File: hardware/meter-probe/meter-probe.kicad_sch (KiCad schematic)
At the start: 49 parts, among them J1 Cable, SW1 Sensor Button, U1 TSL2585, U2 USBLC6-2SC6, U3 MIC5365-1.8YC5, U4 FT260Q, U5 CAT24C08

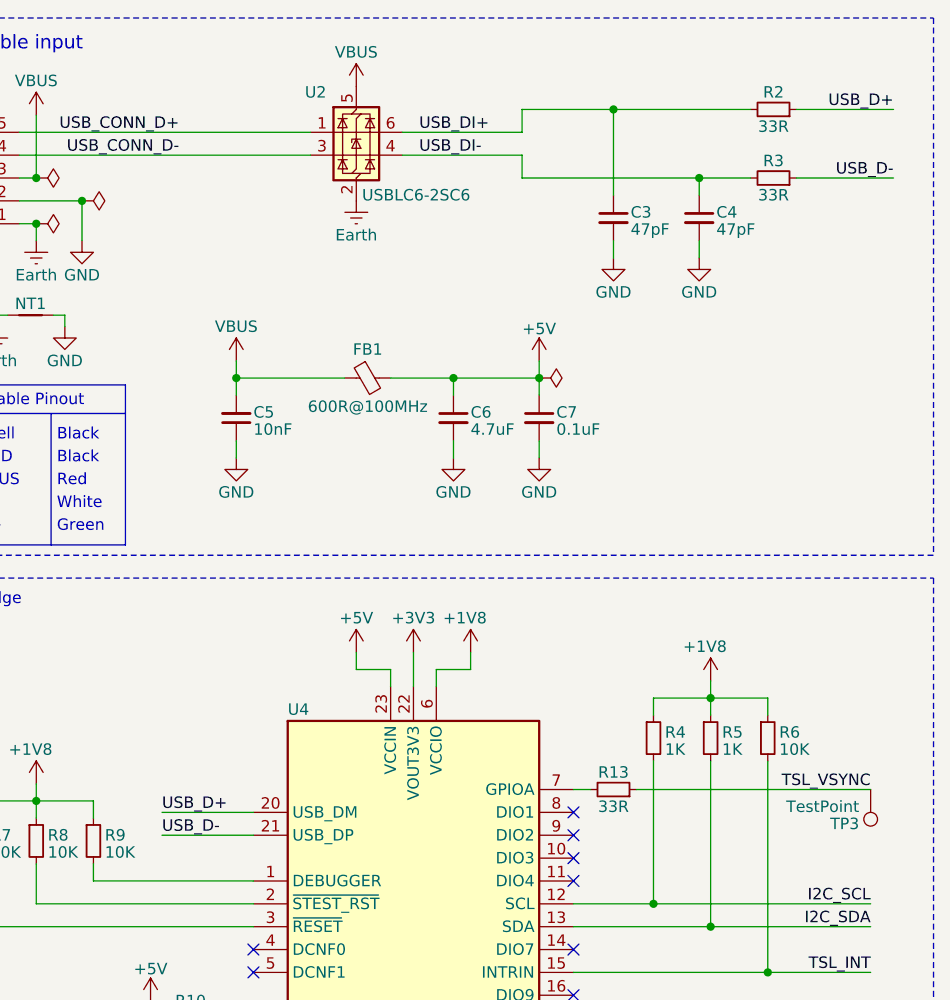
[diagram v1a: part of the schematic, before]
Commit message: Fix pin swap with USB cable connector
This adds vias to the USB traces, which we normally try to avoid, but
that's the only way to route it. Hopefully it won't cause any issues.

Fix #51
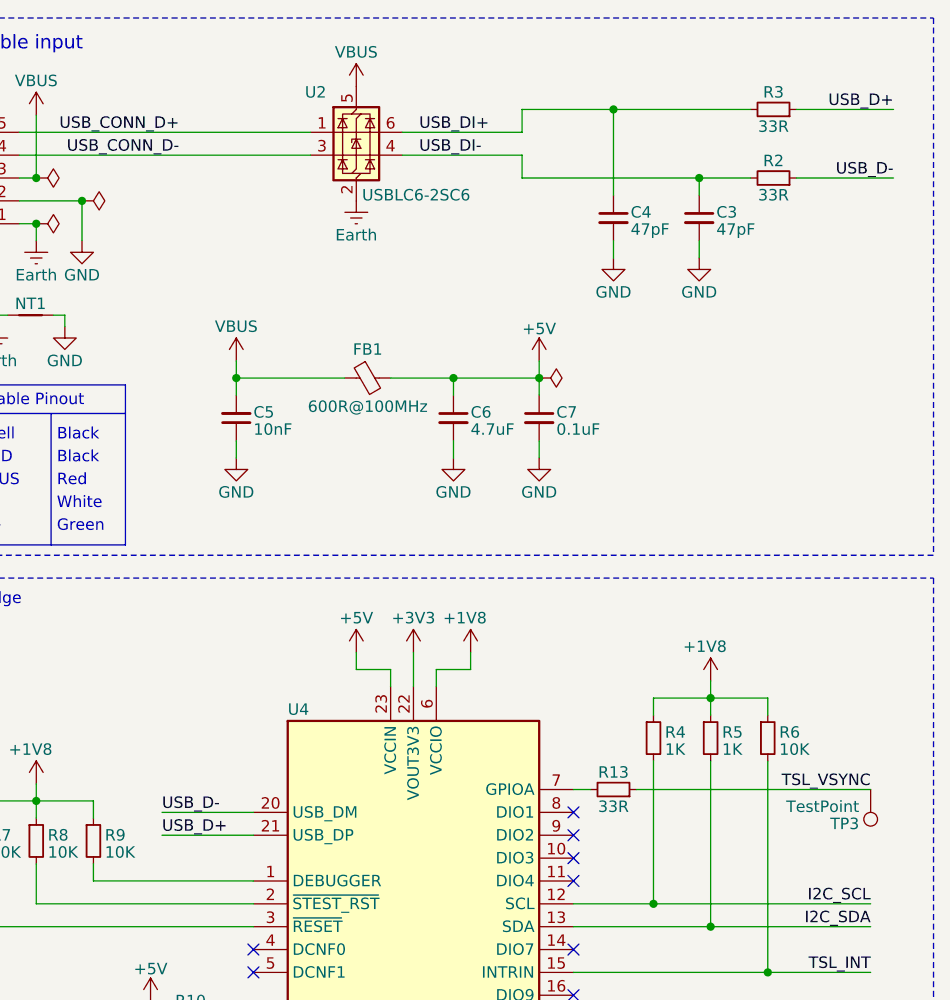
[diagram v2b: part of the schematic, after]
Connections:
- net USB_D+: now also R3.1, U4.21 (USB_DP); no longer R2.1, U4.20 (USB_DM)
- net USB_D-: now also R2.1, U4.20 (USB_DM); no longer R3.1, U4.21 (USB_DP)
- net USB_DI+: now also C4.1, R3.2; no longer C3.1, R2.2
- net USB_DI-: now also C3.1, R2.2; no longer C4.1, R3.2
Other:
- moved on the sheet: C3, C4, R2, R3
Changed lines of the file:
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@@
 	(title_block
 		(title "Printalyzer - Meter Probe")
-		(date "2024-02-27")
+		(date "2024-04-16")
 		(rev "E")
 		(company "Dektronics, Inc.")
@@
 	)
 	(label "USB_D+"
-		(at 41.275 102.87 0)
+		(at 41.275 105.41 0)
 		(fields_autoplaced yes)
 		(effects
@@
 	)
 	(label "USB_D-"
-		(at 41.275 105.41 0)
+		(at 41.275 102.87 0)
 		(fields_autoplaced yes)
 		(effects
@@
 	(symbol
 		(lib_id "Device:C_Small")
-		(at 91.44 36.83 0)
+		(at 100.965 36.83 0)
 		(mirror y)
 		(unit 1)
@@
 		(dnp no)
 		(property "Reference" "C3"
-			(at 93.345 36.195 0)
+			(at 102.87 36.195 0)
 			(effects
 				(font
@@
 		)
 		(property "Value" "47pF"
-			(at 93.345 38.1 0)
+			(at 102.87 38.1 0)
 			(effects
 				(font
@@
 		)
 		(property "Footprint" "Capacitor_SMD:C_0603_1608Metric"
-			(at 91.44 36.83 0)
+			(at 100.965 36.83 0)
 			(effects
 				(font
@@
 		)
 		(property "Datasheet" "https://www.yageo.com/upload/media/product/productsearch/datasheet/mlcc/UPY-GP_NP0_16V-to-50V_18.pdf"
-			(at 91.44 36.83 0)
+			(at 100.965 36.83 0)
 			(effects
 				(font
@@
 		)
 		(property "Description" "CAP CER 47PF 50V C0G/NPO 0603"
-			(at 91.44 36.83 0)
+			(at 100.965 36.83 0)
 			(effects
 				(font
@@
 		)
 		(property "Manufacturer" "YAGEO"
-			(at 91.44 36.83 0)
+			(at 100.965 36.83 0)
 			(effects
 				(font
@@
 		)
 		(property "Manufacturer PN" "CC0603JRNPO9BN470"
-			(at 91.44 36.83 0)
+			(at 100.965 36.83 0)
 			(effects
 				(font
@@
 		)
 		(property "Supplier" "Digi-Key"
-			(at 91.44 36.83 0)
+			(at 100.965 36.83 0)
 			(effects
 				(font
@@
 		)
 		(property "Supplier PN" "311-1065-1-ND"
-			(at 91.44 36.83 0)
+			(at 100.965 36.83 0)
 			(effects
 				(font
@@
 	(symbol
 		(lib_id "Device:C_Small")
-		(at 100.965 36.83 0)
+		(at 91.44 36.83 0)
 		(mirror y)
 		(unit 1)
@@
 		(dnp no)
 		(property "Reference" "C4"
-			(at 102.87 36.195 0)
+			(at 93.345 36.195 0)
 			(effects
 				(font
@@
 		)
 		(property "Value" "47pF"
-			(at 102.87 38.1 0)
+			(at 93.345 38.1 0)
 			(effects
 				(font
@@
 		)
 		(property "Footprint" "Capacitor_SMD:C_0603_1608Metric"
-			(at 100.965 36.83 0)
+			(at 91.44 36.83 0)
 			(effects
 				(font
@@
 		)
 		(property "Datasheet" "https://www.yageo.com/upload/media/product/productsearch/datasheet/mlcc/UPY-GP_NP0_16V-to-50V_18.pdf"
-			(at 100.965 36.83 0)
+			(at 91.44 36.83 0)
 			(effects
 				(font
@@
 		)
 		(property "Description" "CAP CER 47PF 50V C0G/NPO 0603"
-			(at 100.965 36.83 0)
+			(at 91.44 36.83 0)
 			(effects
 				(font
@@
 		)
 		(property "Manufacturer" "YAGEO"
-			(at 100.965 36.83 0)
+			(at 91.44 36.83 0)
 			(effects
 				(font
@@
 		)
 		(property "Manufacturer PN" "CC0603JRNPO9BN470"
-			(at 100.965 36.83 0)
+			(at 91.44 36.83 0)
 			(effects
 				(font
@@
 		)
 		(property "Supplier" "Digi-Key"
-			(at 100.965 36.83 0)
+			(at 91.44 36.83 0)
 			(effects
 				(font
@@
 		)
 		(property "Supplier PN" "311-1065-1-ND"
-			(at 100.965 36.83 0)
+			(at 91.44 36.83 0)
 			(effects
 				(font
@@
 	(symbol
 		(lib_id "Device:R_Small")
-		(at 109.22 24.765 270)
+		(at 109.22 32.385 270)
 		(mirror x)
 		(unit 1)
@@
 		(dnp no)
 		(property "Reference" "R2"
-			(at 109.22 22.86 90)
+			(at 109.22 30.48 90)
 			(effects
 				(font
@@
 		)
 		(property "Value" "33R"
-			(at 109.22 26.67 90)
+			(at 109.22 34.29 90)
 			(effects
 				(font
@@
 		)
 		(property "Footprint" "Resistor_SMD:R_0603_1608Metric"
-			(at 109.22 26.543 90)
+			(at 109.22 34.163 90)
 			(effects
 				(font
@@
 		)
 		(property "Datasheet" "https://www.yageo.com/upload/media/product/productsearch/datasheet/rchip/PYu-RC_Group_51_RoHS_L_12.pdf"
-			(at 109.22 24.765 0)
+			(at 109.22 32.385 0)
 			(effects
 				(font
@@
 		)
 		(property "Description" "RES 33 OHM 5% 1/10W 0603"
-			(at 109.22 24.765 0)
+			(at 109.22 32.385 0)
 			(effects
 				(font
@@
 		)
 		(property "Manufacturer" "YAGEO"
-			(at 109.22 24.765 0)
+			(at 109.22 32.385 0)
 			(effects
 				(font
@@
 		)
 		(property "Manufacturer PN" "RC0603JR-0733RL"
-			(at 109.22 24.765 0)
+			(at 109.22 32.385 0)
 			(effects
 				(font
@@
 		)
 		(property "Supplier" "Digi-Key"
-			(at 109.22 24.765 0)
+			(at 109.22 32.385 0)
 			(effects
 				(font
@@
 		)
 		(property "Supplier PN" "311-33GRCT-ND"
-			(at 109.22 24.765 0)
+			(at 109.22 32.385 0)
 			(effects
 				(font
@@
 	(symbol
 		(lib_id "Device:R_Small")
-		(at 109.22 32.385 270)
+		(at 109.22 24.765 270)
 		(mirror x)
 		(unit 1)
@@
 		(dnp no)
 		(property "Reference" "R3"
-			(at 109.22 30.48 90)
+			(at 109.22 22.86 90)
 			(effects
 				(font
@@
 		)
 		(property "Value" "33R"
-			(at 109.22 34.29 90)
+			(at 109.22 26.67 90)
 			(effects
 				(font
@@
 		)
 		(property "Footprint" "Resistor_SMD:R_0603_1608Metric"
-			(at 109.22 34.163 90)
+			(at 109.22 26.543 90)
 			(effects
 				(font
@@
 		)
 		(property "Datasheet" "https://www.yageo.com/upload/media/product/productsearch/datasheet/rchip/PYu-RC_Group_51_RoHS_L_12.pdf"
-			(at 109.22 32.385 0)
+			(at 109.22 24.765 0)
 			(effects
 				(font
@@
 		)
 		(property "Description" "RES 33 OHM 5% 1/10W 0603"
-			(at 109.22 32.385 0)
+			(at 109.22 24.765 0)
 			(effects
 				(font
@@
 		)
 		(property "Manufacturer" "YAGEO"
-			(at 109.22 32.385 0)
+			(at 109.22 24.765 0)
 			(effects
 				(font
@@
 		)
 		(property "Manufacturer PN" "RC0603JR-0733RL"
-			(at 109.22 32.385 0)
+			(at 109.22 24.765 0)
 			(effects
 				(font
@@
 		)
 		(property "Supplier" "Digi-Key"
-			(at 109.22 32.385 0)
+			(at 109.22 24.765 0)
 			(effects
 				(font
@@
 		)
 		(property "Supplier PN" "311-33GRCT-ND"
-			(at 109.22 32.385 0)
+			(at 109.22 24.765 0)
 			(effects
 				(font

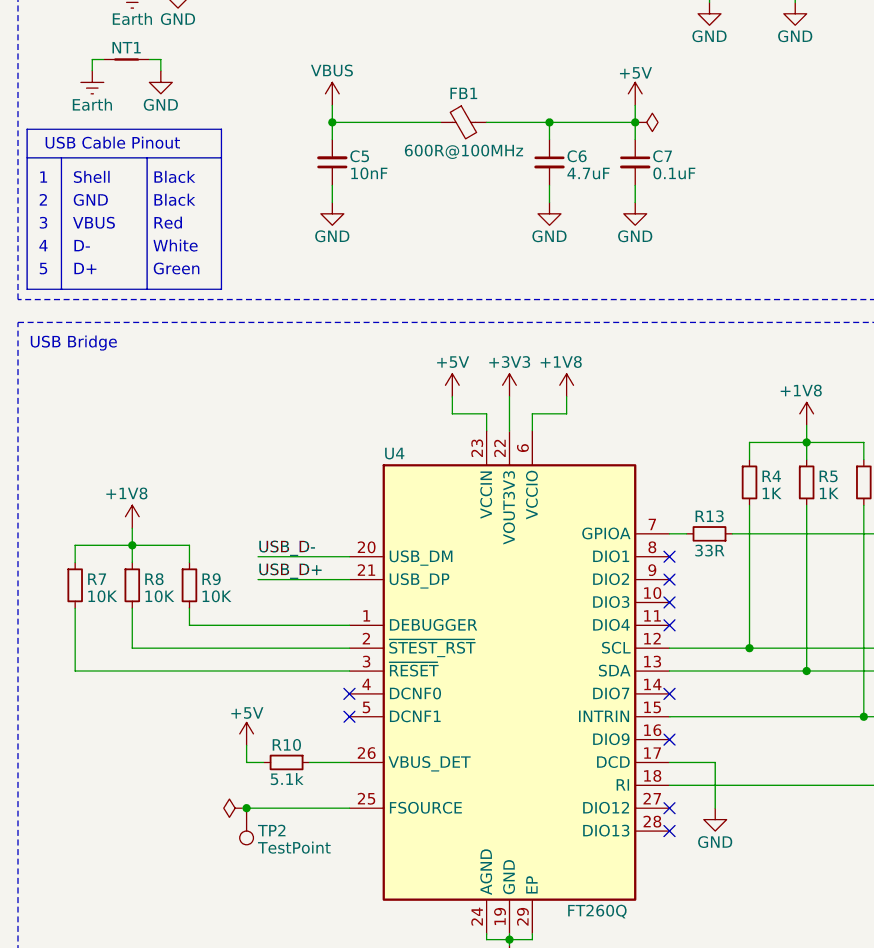
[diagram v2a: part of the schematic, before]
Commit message: Update power input and reset line components
Ref #65
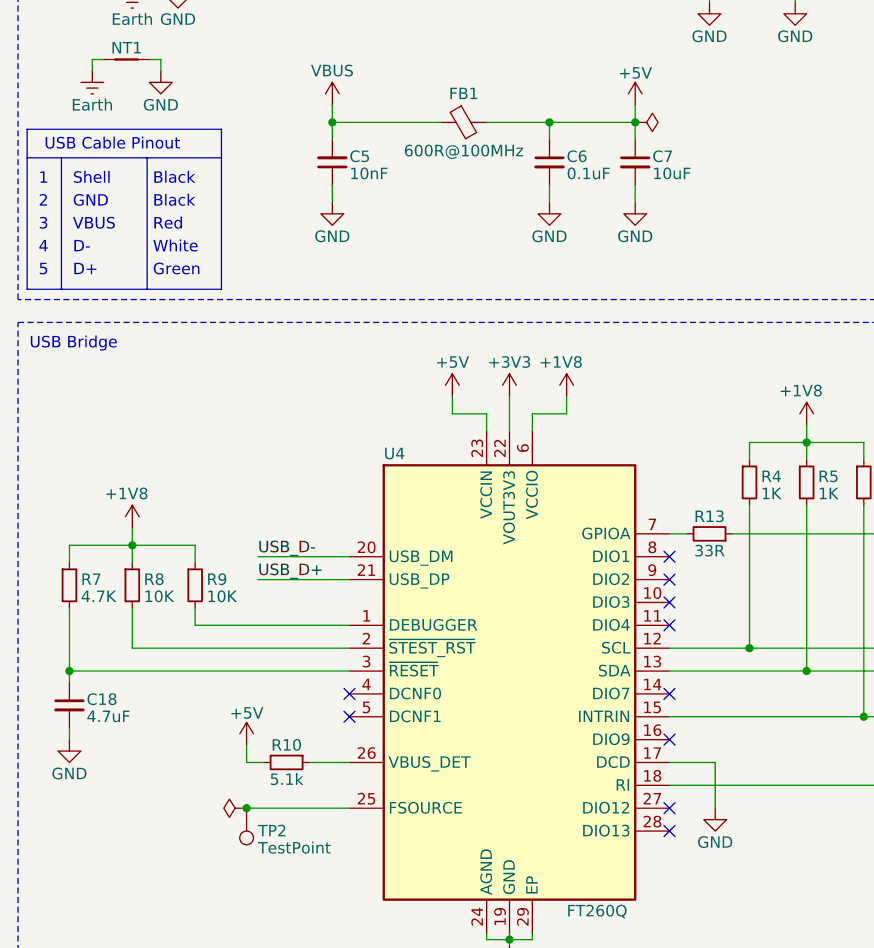
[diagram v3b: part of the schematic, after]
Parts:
- added C18: 4.7uF, Capacitor_SMD:C_0603_1608Metric, symbol Device:C_Small
- C6: value 4.7uF -> 0.1uF; Manufacturer PN CL10A475KA8NQNC -> CL10B104KA8NNNC; Supplier LCSC -> Digi-Key; Supplier PN C69335 -> 1276-1006-1-ND
- C7: value 0.1uF -> 10uF; footprint Capacitor_SMD:C_0603_1608Metric -> Capacitor_SMD:C_0805_2012Metric; Manufacturer PN CL10B104KA8NNNC -> CL21A106KAYNNNE; Supplier PN 1276-1006-1-ND -> 1276-2891-1-ND
- R7: value 10K -> 4.7K; Manufacturer Vishay Dale -> YAGEO; Manufacturer PN CRCW060310K0JNEA -> RC0603JR-074K7L; Supplier PN 541-10KGCT-ND -> 311-4.7KGRCT-ND
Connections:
- net GND: now also C18.2
- net at R7.2, U4.3 (~{RESET}): now also C18.1
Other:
- moved on the sheet: R7, R9

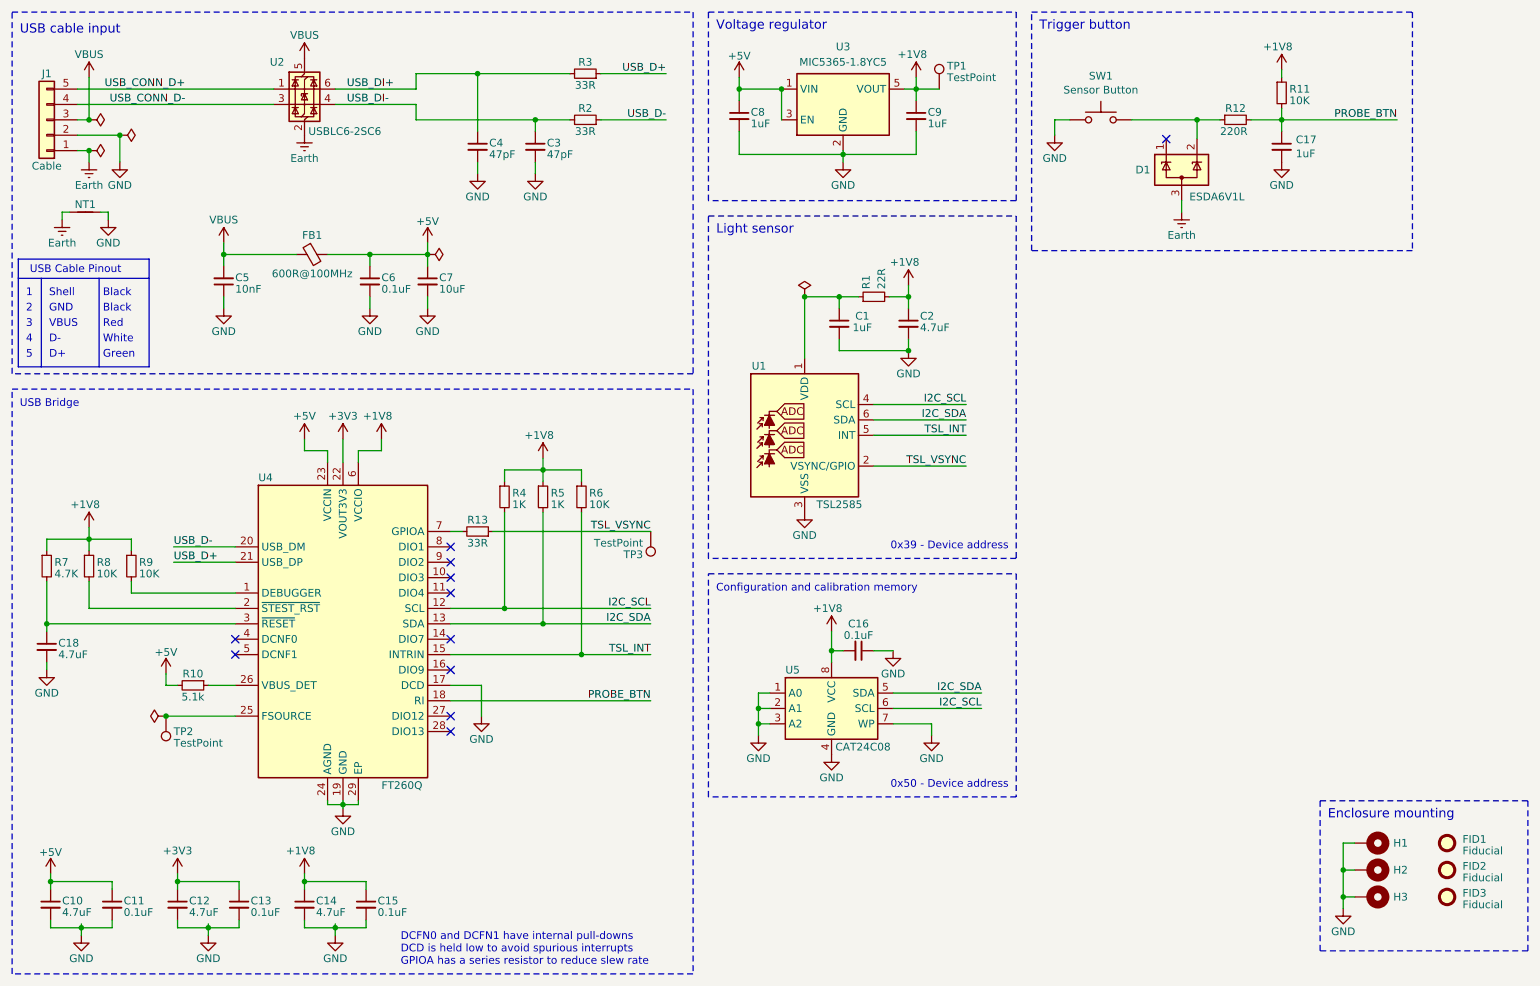
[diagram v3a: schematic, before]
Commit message: Update meter probe power rail setup and layout
This makes the changes noted in the referenced issue, to switch the
FT260 I/O voltage to 3.3V. It also includes numerous minor layout
adjustments.

Ref #65
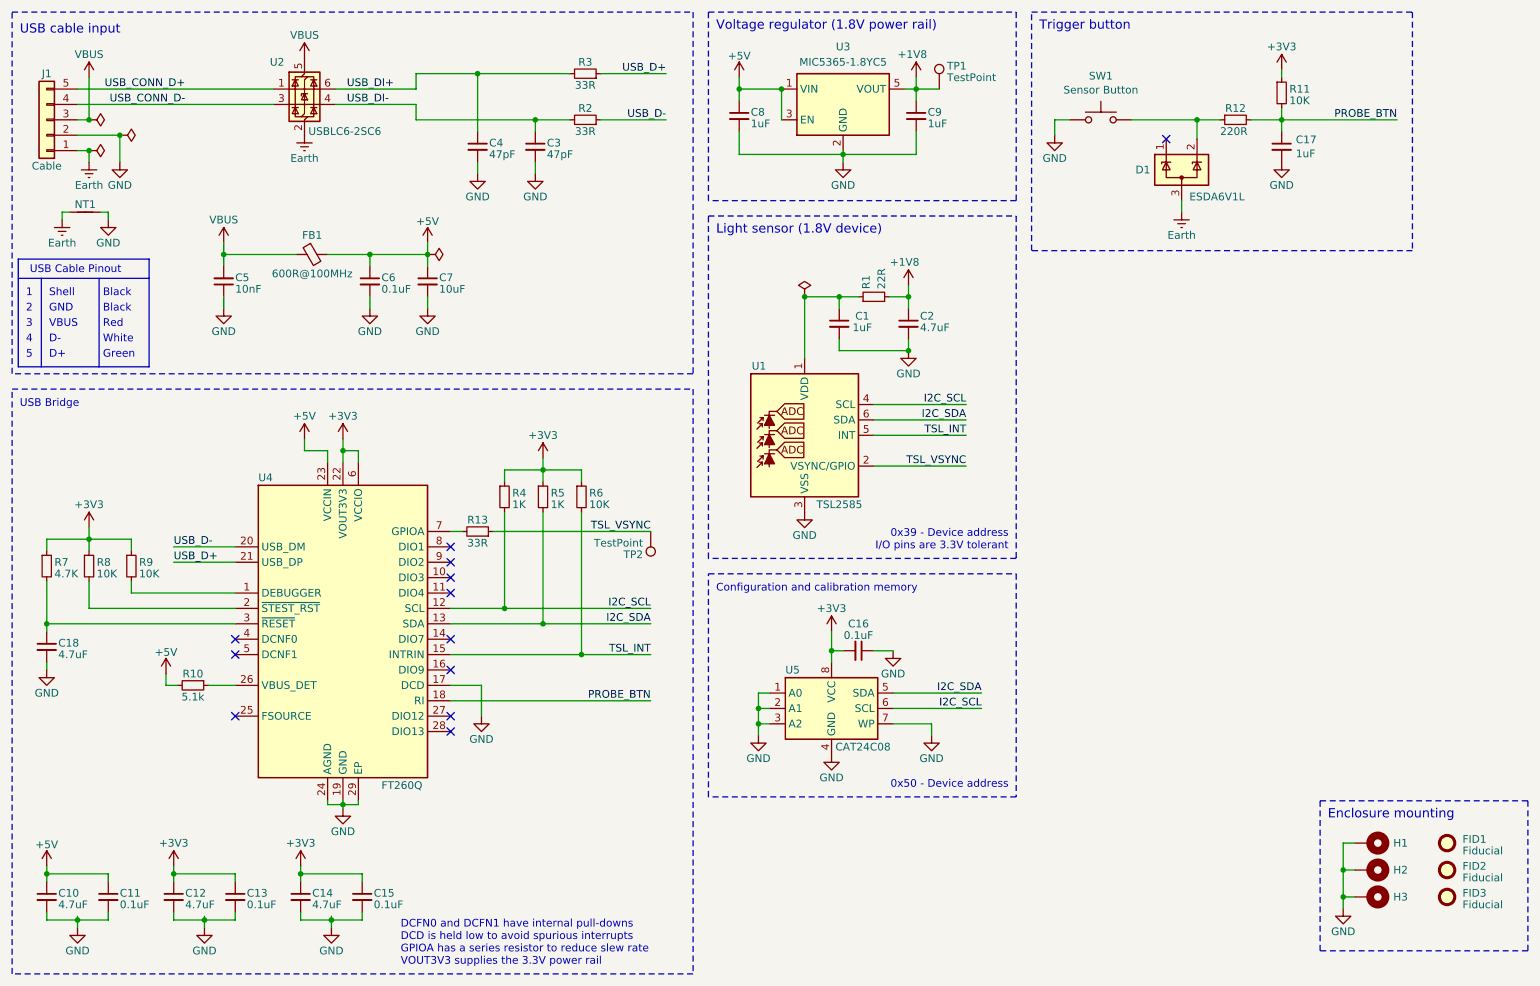
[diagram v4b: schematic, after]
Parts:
- removed TP2: TestPoint, TestPoint:TestPoint_Pad_D1.0mm, symbol Connector:TestPoint
- renumbered TP3 to TP2
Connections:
- net +1V8: no longer C14.1, C15.1, C16.2, R11.1, R4.1, R5.1, R6.1, R7.1, R8.1, R9.1, U4.6 (VCCIO), U5.8 (VCC)
- net +3V3: now also C14.1, C15.1, C16.2, R11.1, R4.1, R5.1, R6.1, R7.1, R8.1, R9.1, U4.6 (VCCIO), U5.8 (VCC)
- no-connect marks 11 -> 12
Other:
- note added: "0x39 - Device address I/O pins are 3.3V tolerant"
- note added: "DCFN0 and DCFN1 have internal pull-downs DCD is held low to avoid spurious interrupts GPIOA has a series resistor to reduce slew rate VOUT3V3 supplies the 3.3V power rail"
- note added: "Light sensor (1.8V device)"
- note added: "Voltage regulator (1.8V power rail)"
- note removed: "0x39 - Device address"
- note removed: "DCFN0 and DCFN1 have internal pull-downs DCD is held low to avoid spurious interrupts GPIOA has a series resistor to reduce slew rate"
- note removed: "Light sensor"
- note removed: "Voltage regulator"
- moved on the sheet: C10, C11, C12, C13, C14, C15
